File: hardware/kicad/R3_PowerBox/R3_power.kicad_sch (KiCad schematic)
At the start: 0 parts

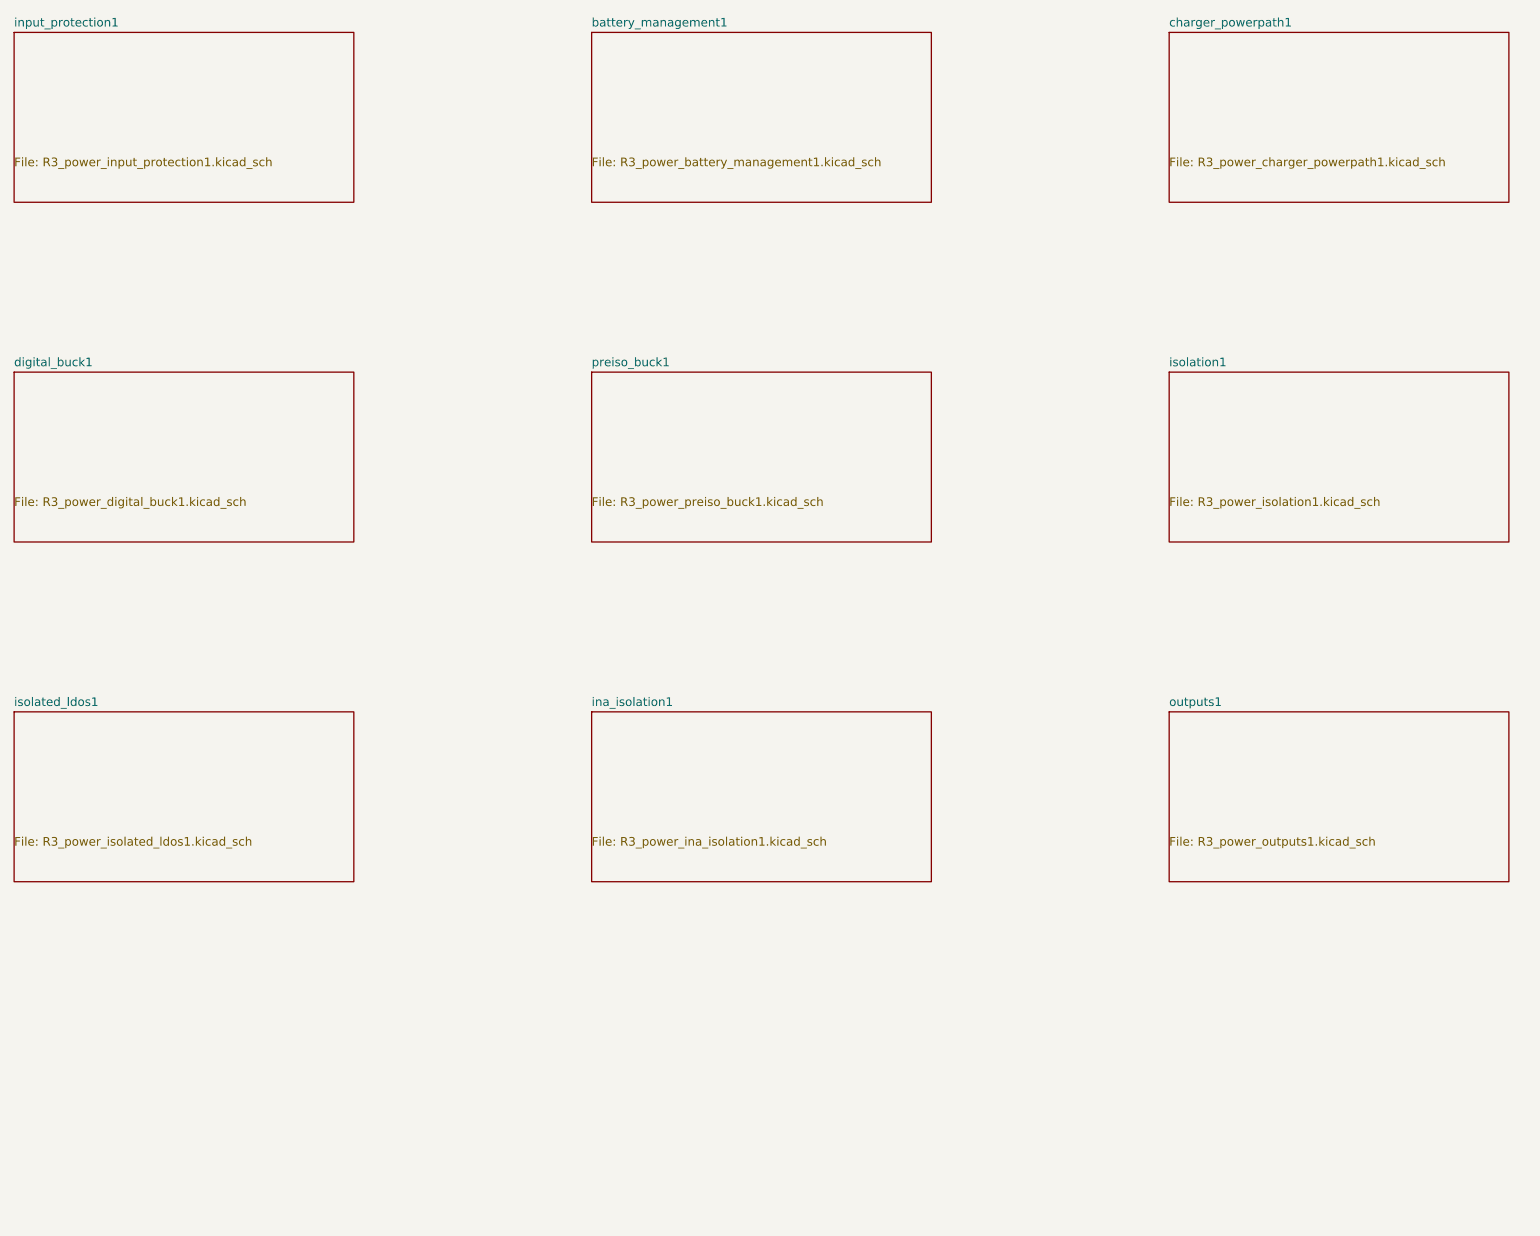
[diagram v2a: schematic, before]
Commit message: Finalize R3 PowerBox user power controls
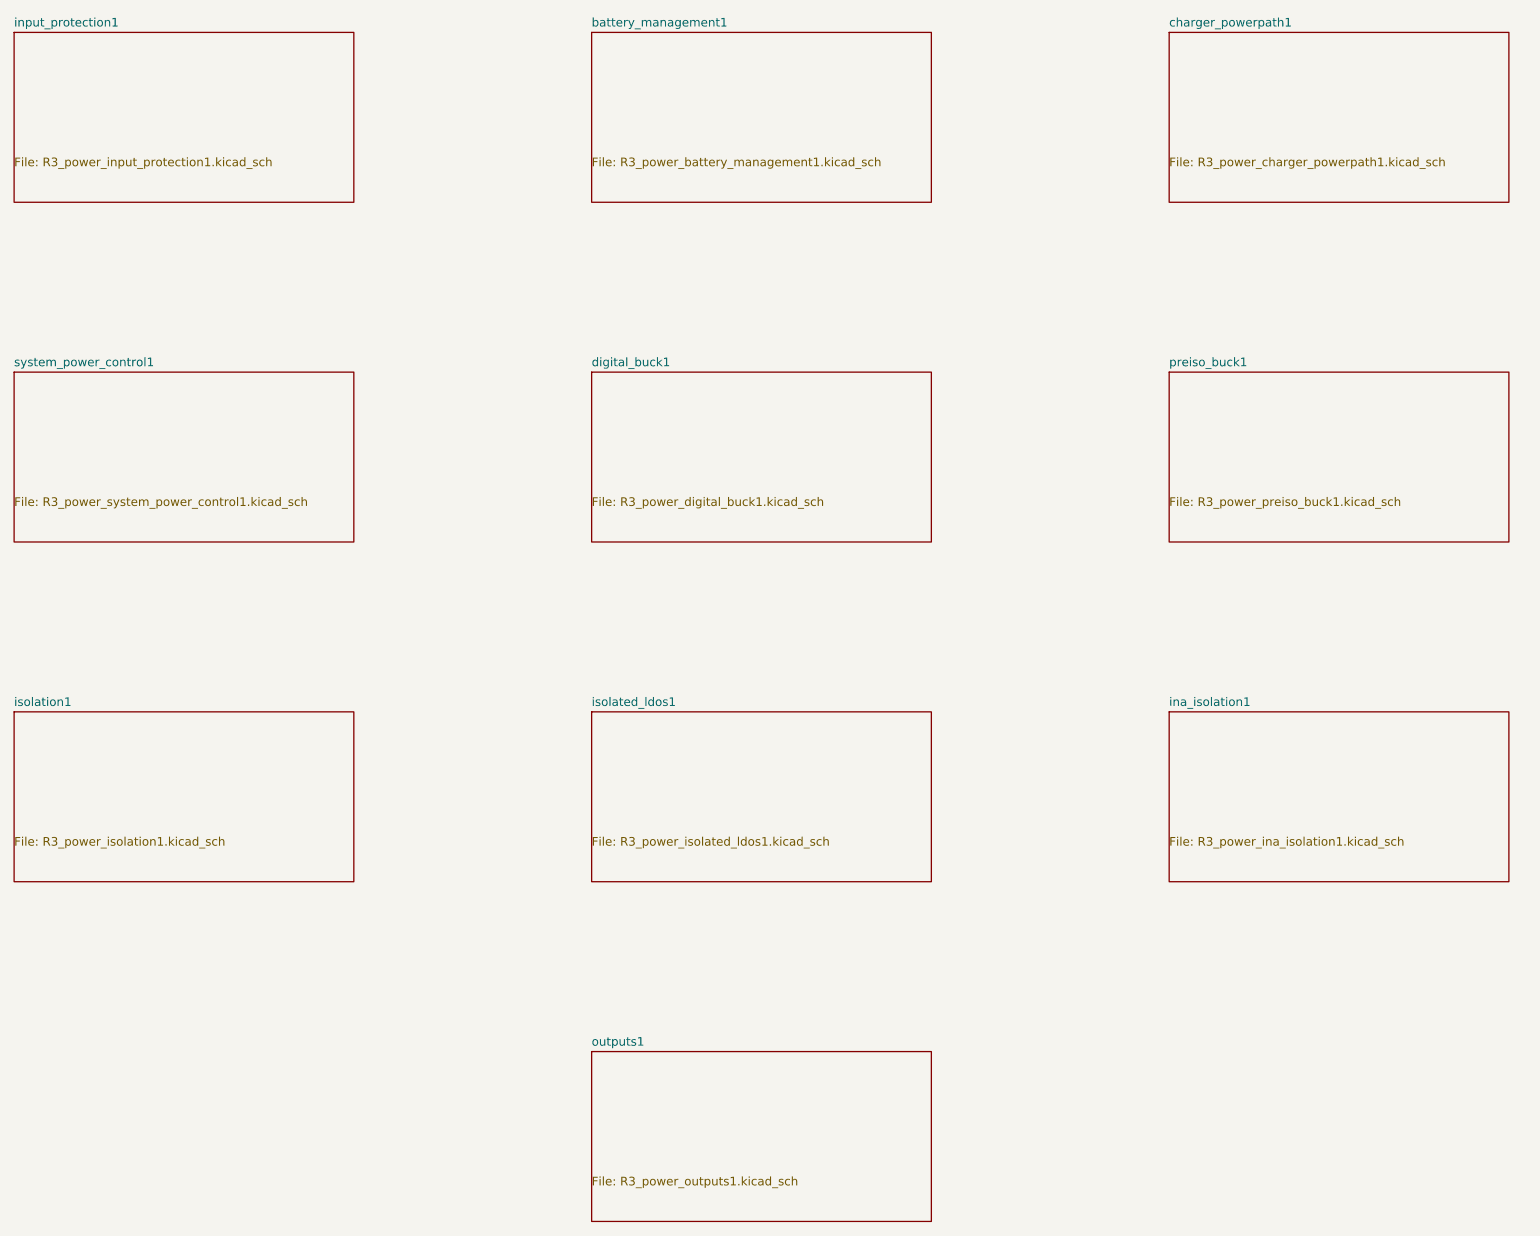
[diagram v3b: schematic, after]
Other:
- added sheet system_power_control1 (R3_power_system_power_control1.kicad_sch)
